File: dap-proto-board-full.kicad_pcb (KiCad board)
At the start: 6 copper layers, 42.2 x 61.4 mm, 102 parts, among them J1 SFV18R-1STE1HLF, J2 UJ20-C-H-G-SMT-1-P16-TR, J3 SJ-3523-SMT, J4 JST_SH_SM03B-SRSS-TB, J5 JST_PH_S2B-PH-SM4, J6 Conn_01x06, J7 Conn_01x08, SW1 B3U-1000P, SW2 B3U-1000P, U1 TPD1E05U06DPY, U10 nPM1300-QEXX, U11 TPS22917DBV, U12 TPS63031DSK, U2 TAD5212, U3 TXS0108ERGYR, U4 W25Q64JWUUIQ, U5 TXS0108ERGYR, U6 MSD-11-A, U7 APS6404L-SQRH-ZR, U8 RP2350A, U9 TLV73311PDBV, Y1 SIT8021AI-J4-XXS-12.288E, Y2 SIT8021AI-J4-XXS-11.289E, Y3 ABM8-272-T3

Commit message: I forgort what I did
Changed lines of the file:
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@@
+	)
+	(segment
+		(start 110.4 81.408102)
+		(end 110.4 81.8)
+		(width 0.150114)
+		(layer "F.Cu")
+		(net "/QSPI_SD2")
+	)
+	(segment
+		(start 109.868955 80.877057)
+		(end 110.4 81.408102)
+		(width 0.150114)
+		(layer "F.Cu")
+		(net "/QSPI_SD2")
 	)
 	(segment
@@
 	)
 	(segment
-		(start 109.868955 80.877057)
-		(end 110.4 81.408102)
-		(width 0.150114)
-		(layer "F.Cu")
-		(net "/QSPI_SD2")
-	)
-	(segment
-		(start 106.470716 80.05722)
-		(end 106.486498 80.073002)
-		(width 0.150114)
-		(layer "F.Cu")
-		(net "/QSPI_SD2")
-	)
-	(segment
-		(start 106.451998 80.073002)
-		(end 106.475 80.05)
+		(start 106.486498 80.073002)
+		(end 106.823874 80.073002)
 		(width 0.150114)
 		(layer "F.Cu")
@@
 	)
 	(segment
-		(start 106.486498 80.073002)
-		(end 106.823874 80.073002)
+		(start 106.486497 80.073001)
+		(end 106.486498 80.073002)
 		(width 0.150114)
 		(layer "F.Cu")
@@
 	)
 	(segment
-		(start 110.4 81.408102)
-		(end 110.4 81.8)
+		(start 106.130949 80.073001)
+		(end 106.486497 80.073001)
+		(width 0.150114)
+		(layer "F.Cu")
+		(net "/QSPI_SD2")
+	)
+	(segment
+		(start 106.451998 80.073002)
+		(end 106.475 80.05)
 		(width 0.150114)
 		(layer "F.Cu")
@@
 	)
 	(via
-		(at 106.470716 80.05722)
+		(at 106.130949 80.073001)
 		(size 0.45)
 		(drill 0.3)
@@
 	)
 	(segment
-		(start 105.973002 80.073002)
-		(end 104 78.1)
+		(start 104 78.1)
+		(end 104 77.55)
 		(width 0.150114)
 		(layer "In2.Cu")
@@
 	)
 	(segment
-		(start 106.470716 80.05722)
-		(end 106.454934 80.073002)
-		(width 0.150114)
-		(layer "In2.Cu")
-		(net "/QSPI_SD2")
-	)
-	(segment
-		(start 106.454934 80.073002)
+		(start 106.130948 80.073002)
 		(end 105.973002 80.073002)
 		(width 0.150114)
@@
 	)
 	(segment
-		(start 104 78.1)
-		(end 104 77.55)
+		(start 106.130949 80.073001)
+		(end 106.130948 80.073002)
 		(width 0.150114)
 		(layer "In2.Cu")
+		(net "/QSPI_SD2")
+	)
+	(segment
+		(start 105.973002 80.073002)
+		(end 104 78.1)
+		(width 0.150114)
+		(layer "In2.Cu")

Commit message: mostly finished; just need to breakout extra gpio
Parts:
- removed C19, C40, C48, C52: 100nF, Capacitor_SMD:C_0402_1005Metric
- removed C41, C43: 10uF, Capacitor_SMD:C_0603_1608Metric
- removed C42, C44: 100nF, Capacitor_SMD:C_0603_1608Metric
- removed C45, C46, C51, C53, C54: 10uF, Capacitor_SMD:C_0402_1005Metric
- removed C47: 2.2uF, Capacitor_SMD:C_0402_1005Metric
- removed C49: 1uF, Capacitor_SMD:C_0402_1005Metric
- removed C50: 1nF, Capacitor_SMD:C_0402_1005Metric
- removed J5: JST_PH_S2B-PH-SM4, Connector_JST:JST_PH_S2B-PH-SM4-TB_1x02-1MP_P2.00mm_Horizontal
- removed J6: Conn_01x06, Connector_PinSocket_2.54mm:PinSocket_1x06_P2.54mm_Vertical
- removed J7: Conn_01x08, Connector_PinSocket_2.54mm:PinSocket_1x08_P2.54mm_Vertical
- removed L1: 2.2uH, Inductor_SMD:L_0603_1608Metric
- removed R14: 4.7k, Resistor_SMD:R_0402_1005Metric
- removed R15: 10, Resistor_SMD:R_0402_1005Metric
- removed R16: 47k, Resistor_SMD:R_0402_1005Metric
- removed R3: 10k, Resistor_SMD:R_0402_1005Metric
- removed U10: nPM1300-QEXX, Package_DFN_QFN:QFN-32-1EP_5x5mm_P0.5mm_EP3.6x3.6mm_ThermalVias
- removed U11: TPS22917DBV, Package_TO_SOT_SMD:SOT-23-6
- removed U12: TPS63031DSK, Package_SON:WSON-10-1EP_2.5x2.5mm_P0.5mm_EP1.2x2mm_ThermalVias
- removed U8: RP2350A, Package_DFN_QFN:QFN-60-1EP_7x7mm_P0.4mm_EP3.4x3.4mm
- removed U9: TLV73311PDBV, Package_TO_SOT_SMD:SOT-23-5
- removed Y2: SIT8021AI-J4-XXS-11.289E, SIT8021AI-J4-XXS-24.000000E:OSC_SIT8021AI-J4-XXS-24.000000E
- removed Y3: ABM8-272-T3, Crystal:Crystal_SMD_3225-4Pin_3.2x2.5mm
- added SW3: B3U-1000P, Button_Switch_SMD:SW_Push_1P1T_NO_Vertical_Wuerth_434133025816, F.Cu at (131.5, 70.1)
- C1, C11, C12, C2, C20, C22, C28, C3, C4, C8, C9: footprint Capacitor_SMD:C_0402_1005Metric -> Capacitor_SMD:C_0603_1608Metric
- C10, C24, C27, C29, C6: value 100nF -> 10uF; footprint Capacitor_SMD:C_0402_1005Metric -> Capacitor_SMD:C_0603_1608Metric
- C13: value 100nF -> 22uF; footprint Capacitor_SMD:C_0402_1005Metric -> Capacitor_SMD:C_0603_1608Metric
- C14: value 10uF -> 10nF; footprint Capacitor_SMD:C_0402_1005Metric -> Capacitor_SMD:C_0603_1608Metric
- C15, C21, C23, C25, C34, C7: value 100nF -> 1uF; footprint Capacitor_SMD:C_0402_1005Metric -> Capacitor_SMD:C_0603_1608Metric
- C16: value 10uF -> 100nF; footprint Capacitor_SMD:C_0402_1005Metric -> Capacitor_SMD:C_0603_1608Metric
- C17: value 1uF -> 18pF; footprint Capacitor_SMD:C_0402_1005Metric -> Capacitor_SMD:C_0603_1608Metric
- C18: value 10nF -> 18pF; footprint Capacitor_SMD:C_0402_1005Metric -> Capacitor_SMD:C_0603_1608Metric
- C26: value 10nF -> 100nF; footprint Capacitor_SMD:C_0402_1005Metric -> Capacitor_SMD:C_0603_1608Metric
- C30: value 15pF -> 100nF; footprint Capacitor_SMD:C_0402_1005Metric -> Capacitor_SMD:C_0603_1608Metric
- C31: value 15pF -> 10uF; footprint Capacitor_SMD:C_0402_1005Metric -> Capacitor_SMD:C_0603_1608Metric
- C32: value 100nF -> 2.2uF; footprint Capacitor_SMD:C_0402_1005Metric -> Capacitor_SMD:C_0603_1608Metric
- C33: value 4.7uF -> 100nF; footprint Capacitor_SMD:C_0402_1005Metric -> Capacitor_SMD:C_0603_1608Metric
- C35: value 10uF -> 1nF; footprint Capacitor_SMD:C_0402_1005Metric -> Capacitor_SMD:C_0603_1608Metric
- C36: value 2.2uF -> 10uF; footprint Capacitor_SMD:C_0402_1005Metric -> Capacitor_SMD:C_0603_1608Metric
- C37: value 1uF -> 100nF; footprint Capacitor_SMD:C_0402_1005Metric -> Capacitor_SMD:C_0603_1608Metric
- C38, C39: value 1uF -> 10uF; footprint Capacitor_SMD:C_0402_1005Metric -> Capacitor_SMD:C_0603_1608Metric
- C5: value 13pF -> 100nF; footprint Capacitor_SMD:C_0402_1005Metric -> Capacitor_SMD:C_0603_1608Metric
- J4: value JST_SH_SM03B-SRSS-TB -> JST_PH_S2B-PH-SM4; footprint Connector_JST:JST_SH_SM03B-SRSS-TB_1x03-1MP_P1.00mm_Horizontal -> Connector_JST:JST_PH_S2B-PH-SM4-TB_1x02-1MP_P2.00mm_Horizontal
- R1: value 100k -> 0; footprint Resistor_SMD:R_0402_1005Metric -> Resistor_SMD:R_0603_1608Metric
- R10, R11, R12: value 4.7k -> 47k; footprint Resistor_SMD:R_0402_1005Metric -> Resistor_SMD:R_0603_1608Metric
- R13: value 1k -> 47k; footprint Resistor_SMD:R_0402_1005Metric -> Resistor_SMD:R_0603_1608Metric
- R2: value 100k -> 10k; footprint Resistor_SMD:R_0402_1005Metric -> Resistor_SMD:R_0603_1608Metric
- R4: value 10k -> 2.2; footprint Resistor_SMD:R_0402_1005Metric -> Resistor_SMD:R_0603_1608Metric
- R5, R6: footprint Resistor_SMD:R_0402_1005Metric -> Resistor_SMD:R_0603_1608Metric
- R7: value 1k -> 10k; footprint Resistor_SMD:R_0402_1005Metric -> Resistor_SMD:R_0603_1608Metric
- R8, R9: value 27 -> 10k; footprint Resistor_SMD:R_0402_1005Metric -> Resistor_SMD:R_0603_1608Metric
- SW1, SW2: value B3U-1000P -> SW_Push; footprint Button_Switch_SMD:SW_SPST_B3U-1000P -> Button_Switch_SMD:SW_Push_1P1T_NO_Vertical_Wuerth_434133025816
- U1: value TPD1E05U06DPY -> MSD-11-A; footprint Package_SON:Texas_DPY0002A_0.6x1mm_P0.65mm -> MSD-11-A:CUI_MSD-11-A
- U2: value TAD5212 -> USBLC6-2SC6; footprint Package_DFN_QFN:TAD5212 -> Package_TO_SOT_SMD:SOT-23-6
- U3: value TXS0108ERGYR -> TAD5212; footprint Package_DFN_QFN:Texas_RGY_R-PVQFN-N20_EP2.05x3.05mm_ThermalVias -> footprints:VQFN24_RGE_CORNERPADS_TEX
- U4: value W25Q64JWUUIQ -> ESP32-S3; footprint Package_SON:Winbond_USON-8-1EP_3x2mm_P0.5mm_EP0.2x1.6mm -> Package_DFN_QFN:QFN-56-1EP_7x7mm_P0.4mm_EP4x4mm_ThermalVias
- U5: value TXS0108ERGYR -> nPM1300-QEXX; footprint Package_DFN_QFN:Texas_RGY_R-PVQFN-N20_EP2.05x3.05mm_ThermalVias -> Package_DFN_QFN:QFN-32-1EP_5x5mm_P0.5mm_EP3.6x3.6mm_ThermalVias
- U6: value MSD-11-A -> TPS22917DBV; footprint MSD-11-A:CUI_MSD-11-A -> Package_TO_SOT_SMD:SOT-23-6
- U7: value APS6404L-SQRH-ZR -> TPS63031DSK; footprint Package_SON:Winbond_USON-8-1EP_3x2mm_P0.5mm_EP0.2x1.6mm -> Package_SON:WSON-10-1EP_2.5x2.5mm_P0.5mm_EP1.2x2mm_ThermalVias
- Y1: value SIT8021AI-J4-XXS-12.288E -> ABM8-40.000MHZ-12-B1U-T; footprint SIT8021AI-J4-XXS-24.000000E:OSC_SIT8021AI-J4-XXS-24.000000E -> Crystal:Crystal_SMD_3225-4Pin_3.2x2.5mm
- moved J4 51.3 mm to (129.6, 62.4)
- moved U1 39.0 mm to (103.1, 103.6)
- moved H2 37.0 mm to (130.7, 75.6)
- moved R4 34.0 mm to (126.7, 105.4)
- moved C9 32.3 mm to (126.7, 101.9), turned to 180 degrees
- moved C31 30.2 mm to (121.2, 64.1), turned to 0 degrees
- moved R2 29.2 mm to (132.3, 87.9)
- moved C35 27.2 mm to (113.9, 101.0), turned to 0 degrees
- moved U2 26.9 mm to (112.6, 66.7)
- moved C33 26.4 mm to (121.2, 65.7), turned to 0 degrees
- moved C26 25.7 mm to (125.4, 70.2), turned to 0 degrees
- moved C32 25.3 mm to (124.4, 66.0), turned to 0 degrees
- moved SW1 23.6 mm to (128.1, 82.2), turned to -90 degrees
- moved U5 23.3 mm to (120.4, 69.8), turned to 90 degrees
- moved U3 22.6 mm to (125.4, 98.4), turned to 180 degrees
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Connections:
- C1 pad 2: +1V8 -> +3V3
- C10 pad 1: +3V3 -> GND
- C10 pad 2: GND -> Net-(U3-AVDD)
- C12 pad 1: Net-(U2-VREF) -> +3V3
- C13 pad 1: GND -> +3V3
- C13 pad 2: +1V8 -> GND
- C14 pad 1: GND -> +3V3
- C14 pad 2: +1V8 -> GND
- C15 pad 1: /SD_VCC -> +3V3
- C16 pad 1: /SD_VCC -> +3V3
- C17 pad 1: +1V8 -> /XOUT
- C18 pad 1: +1V8 -> Net-(C18-Pad1)
- C2 pad 1: +1V8 -> +3V3
- C20 pad 1: GND -> +3V3
- C20 pad 2: +1V8 -> GND
- C21 pad 1: GND -> +3V3
- C21 pad 2: +3V3 -> GND
- C22 pad 1: GND -> +3V3
- C22 pad 2: +1V8 -> GND
- C23 pad 1: GND -> Net-(U4-CHIP_PU)
- C23 pad 2: +1V8 -> GND
- C24 pad 1: GND -> +3V3
- C24 pad 2: +1V8 -> GND
- C25 pad 1: GND -> VBUS
- C25 pad 2: +1V8 -> GND
- C26 pad 1: +1V8 -> +3V3
- C27 pad 1: GND -> VSYS
- C27 pad 2: +1V8 -> GND
- C28 pad 1: GND -> VSYS
- C28 pad 2: +1V8 -> GND
- C29 pad 1: GND -> VSYS
- C29 pad 2: +1V8 -> GND
- C30 pad 1: /XIN -> VSYS
- C31 pad 1: Net-(C31-Pad1) -> VSYS
- C32 pad 1: +1V1 -> +BATT
- C33 pad 1: +1V1 -> VSYS
- C34 pad 1: +1V1 -> Net-(U5-VBUSOUT)
- C35 pad 1: +1V8 -> +3V3
- C35 pad 2: GND -> Net-(U6-CT)
- C36 pad 1: /VREG_AVDD -> VSYS
- C37 pad 1: VBUS -> Net-(U7-EN)
- C38 pad 1: +1V8 -> +3V3
- C39 pad 1: +1V1 -> +3V3
- C5 pad 1: /GPO1 -> SD_VCC
- C5 pad 2: Net-(U2-GPO1) -> GND
- C6 pad 1: +1V8 -> SD_VCC
- C7 pad 1: +1V8 -> Net-(U3-MICBIAS)
- C8 pad 1: Net-(U2-MICBIAS) -> Net-(U3-VREF)
- C9 pad 1: +1V8 -> GND
- C9 pad 2: GND -> Net-(U3-AVDD)
- D1 pad 2: +1V8 -> +3V3
- D2 pad 2: +1V8 -> +3V3
- J1 pad 13: /disp_CS_SCL -> /disp_SCL
- J1 pad 14: /disp_DC_SDA -> /disp_SDA
- J1 pad 4: /disp_SCK -> /disp_SCLK
- J1 pad 7: /disp_DC_SDA -> /disp_DC
- J1 pad 9: /disp_CS_SCL -> /disp_CS
- J2 pad A6: /USB_D+ -> Net-(J2-D+-PadA6)
- J2 pad A7: /USB_D- -> Net-(J2-D--PadA7)
- J2 pad B6: /USB_D+ -> Net-(J2-D+-PadA6)
- J2 pad B7: /USB_D- -> Net-(J2-D--PadA7)
- J4 pad 1: /SWCLK -> +BATT
- L2 pad 1: Net-(U12-L1) -> Net-(U7-L1)
- L2 pad 2: Net-(U12-L2) -> Net-(U7-L2)
- R1 pad 1: /SD_ON -> /XIN
- R1 pad 2: GND -> Net-(C18-Pad1)
- R10 pad 1: +1V8 -> +3V3
- R10 pad 2: /npm_SDA -> /npm_SCL
- R11 pad 1: +1V8 -> +3V3
- R11 pad 2: /npm_SCL -> /npm_SDA
- R12 pad 1: +1V8 -> +3V3
- R13 pad 1: /XOUT -> +3V3
- R13 pad 2: Net-(C31-Pad1) -> /tad_SCL
- R2 pad 1: /DISP_IO_ON -> +3V3
- R2 pad 2: GND -> Net-(U4-CHIP_PU)
- R4 pad 1: +1V8 -> +3V3
- R4 pad 2: /PSRAM_CS -> Net-(U3-AVDD)
- R5 pad 1: +1V8 -> +3V3
- R5 pad 2: /DIS_CLK1 -> /SD_DAT2
- R6 pad 1: +1V8 -> +3V3
- R6 pad 2: /DIS_CLK2 -> /SD_CS
- R7 pad 1: /FLASH_CS -> +3V3
- R7 pad 2: /~{USB_BOOT} -> /SD_DIN
- R8 pad 1: /USB_D- -> +3V3
- R8 pad 2: Net-(U8-USB_DM) -> /SD_DOUT
- R9 pad 1: /USB_D+ -> +3V3
- R9 pad 2: Net-(U8-USB_DP) -> /SD_DAT1
- SW1 pad 2: /~{USB_BOOT} -> Net-(U4-GPIO0)
- SW2 pad 1: /SHPHLD -> Net-(U4-CHIP_PU)
- U1 pad 1: GND -> /SD_DAT2
- U1 pad 2: VBUS -> /SD_CS
- U2 pad 1: /DREG -> Net-(J2-D--PadA7)
- U2 pad 2: /BCLK -> GND
- U2 pad 3: /FSYNC -> Net-(J2-D+-PadA6)
- U2 pad 4: /DOUT -> /USB_D+
- U2 pad 5: /DIN -> VBUS
- U2 pad 6: +1V8 -> /USB_D-
- U3 pad 1: /SD_DAT2 -> /DREG
- U3 pad 10: /SD_ON -> /tad_GPIO2
- U3 pad 11: GND -> /tad_GPO1
- U3 pad 12: unconnected-(U3-B8-Pad12) -> /tad_GPI1
- U3 pad 13: unconnected-(U3-B7-Pad13) -> GND
- U3 pad 14: /3v_SD_DAT1 -> Net-(U3-MICBIAS)
- U3 pad 15: /3v_SD_DOUT -> GND
- U3 pad 16: /3v_SD_SCLK -> GND
- U3 pad 17: /3v_SD_DIN -> GND
- U3 pad 18: /3v_SD_CS -> GND
- U3 pad 19: +3V3 -> VCOM
- U3 pad 2: +1V8 -> /BCLK
- U3 pad 20: /3v_SD_DAT2 -> /OUT1P
- U3 pad 21: GND -> /OUT2P
- U3 pad 3: /SD_CS -> /FSYNC
- U3 pad 4: /SD_DIN -> /DOUT
- U3 pad 5: /SD_SCLK -> /DIN
- U3 pad 6: /SD_DOUT -> +3V3
- U3 pad 7: /SD_DAT1 -> /tad_SCL
- U3 pad 8: unconnected-(U3-A7-Pad8) -> /tad_SDA
- U3 pad 9: unconnected-(U3-A8-Pad9) -> /tad_GPIO1
- U4 pad 1: /FLASH_CS -> unconnected-(U4-LNA_IN-Pad1)
- U4 pad 2: /QSPI_SD1 -> +3V3
- U4 pad 3: /QSPI_SD2 -> +3V3
- U4 pad 4: GND -> Net-(U4-CHIP_PU)
- U4 pad 5: /QSPI_SD0 -> Net-(U4-GPIO0)
- U4 pad 6: /QSPI_SCLK -> /tad_SDA
- U4 pad 7: /QSPI_SD3 -> /tad_SCL
- U4 pad 8: +1V8 -> unconnected-(U4-GPIO3-Pad8)
- U4 pad 9: GND -> /DIN
- U5 pad 1: unconnected-(U5-A1-Pad1) -> VSYS
- U5 pad 10: /DISP_IO_ON -> /npm_GPIO3
- U5 pad 11: GND -> /npm_GPIO4
- U5 pad 12: /disp_LITE -> +3V3
- U5 pad 13: /disp_SCK -> /npm_SDA
- U5 pad 14: /disp_MOSI -> /npm_SCL
- U5 pad 15: /disp_MISO -> /SHPHLD
- U5 pad 16: /disp_DC_SDA -> GND
- U5 pad 17: /disp_CS_SCL -> GND
- U5 pad 18: unconnected-(U5-B2-Pad18) -> GND
- U5 pad 19: +3V3 -> +BATT
- U5 pad 2: +1V8 -> GND
- U5 pad 20: unconnected-(U5-B1-Pad20) -> VSYS
- U5 pad 21: GND -> VBUS
- U5 pad 4: /mcu_disp_CS_SCL -> VSYS
- U5 pad 5: /mcu_dsp_DC_SDA -> unconnected-(U5-SW2-Pad5)
- U5 pad 6: /mcu_disp_MISO -> GND
- U5 pad 7: /mcu_disp_MOSI -> /npm_GPIO0
- U5 pad 8: /mcu_disp_SCK -> /npm_GPIO1
- U5 pad 9: /mcu_disp_LITE -> /npm_GPIO2
- U6 pad 1: /3v_SD_DAT2 -> +3V3
- U6 pad 2: /3v_SD_CS -> GND
- U6 pad 3: /3v_SD_DIN -> /SD_ON
- U6 pad 4: /SD_VCC -> Net-(U6-CT)
- U6 pad 5: /3v_SD_SCLK -> SD_VCC
- U6 pad 6: GND -> SD_VCC
- U7 pad 1: /PSRAM_CS -> +3V3
- U7 pad 2: /QSPI_SD1 -> Net-(U7-L2)
- U7 pad 3: /QSPI_SD2 -> GND
- U7 pad 4: GND -> Net-(U7-L1)
- U7 pad 5: /QSPI_SD0 -> VSYS
- U7 pad 6: /QSPI_SCLK -> Net-(U7-EN)
- U7 pad 7: /QSPI_SD3 -> Net-(U7-EN)
- U7 pad 8: +1V8 -> Net-(U7-EN)
- Y1 pad 1: /DIS_CLK1 -> /XOUT
- Y1 pad 2: /GPO1 -> GND
- Y1 pad 3: +1V8 -> Net-(C18-Pad1)
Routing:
- net GND: track 58.3 -> 117.2 mm, vias 133 -> 67
- net +1V8: track 54.1 -> 0.00 mm, vias 35 -> 0
- net /DOUT: track 0.00 -> 33.2 mm
- net /SWCLK: track 32.9 -> 0.00 mm, vias 2 -> 0
- net /SWD: track 30.6 -> 0.00 mm, vias 2 -> 0
- net Net-(U4-CHIP_PU): track 0.00 -> 26.2 mm, vias 0 -> 2
- net /GPIO11: track 26.2 -> 0.00 mm, vias 1 -> 0
- net /GPIO10: track 24.2 -> 0.00 mm
- net /npm_GPIO0: track 22.5 -> 0.00 mm, vias 3 -> 0
- net +3V3: track 9.59 -> 31.9 mm, vias 16 -> 28
- net /BCLK: track 15.4 -> 37.5 mm
- net /GPIO25: track 21.2 -> 0.00 mm, vias 1 -> 0
- net /GPIO26_ADC0: track 21.1 -> 0.00 mm, vias 1 -> 0
- net /FSYNC: track 14.5 -> 35.4 mm
- net /GPIO9: track 22.2 -> 1.58 mm, vias 0 -> 1
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- added copper zone on F.Cu, net /DREG
- added copper zone on F.Cu, net Net-(U3-AVDD)
- added copper zone on F.Cu, net Net-(U3-VREF)
- added copper zone on F.Cu, net SD_VCC
- added copper zone on In2.Cu, net SD_VCC
- added copper zone on In2.Cu, net VSYS
- removed copper zone on In4.Cu, net +1V1
- removed copper zone on F.Cu, net +1V8
- removed copper zone on In4.Cu, net +1V8
- removed copper zone on F.Cu, net +BATT
- removed copper zone on In2.Cu, net /SD_VCC
- removed copper zone on In3.Cu, net GND
- removed copper zone on F.Cu, net VCOM
- removed copper zone on In2.Cu, net VCOM
- removed copper zone on In4.Cu, net VSYS
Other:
- copper layers 6 -> 4
- board text added: "Full DAP Proto Board v2 2026 Isaiah Gamble"
- board text removed: "DEBUG"
- board text removed: "Full DAP Proto Board v1 2026 Isaiah Gamble"

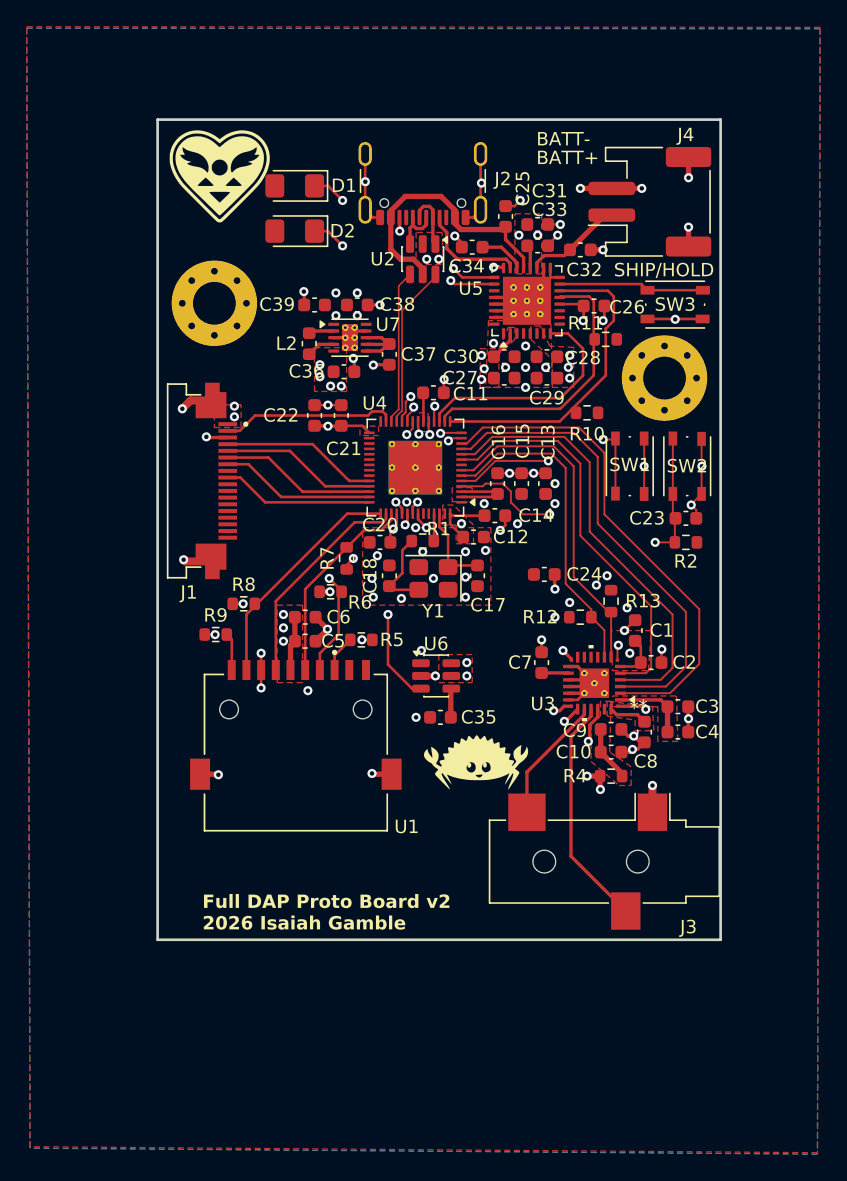
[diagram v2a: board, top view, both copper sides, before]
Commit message: breakout extra gpios; gen gerbers and images
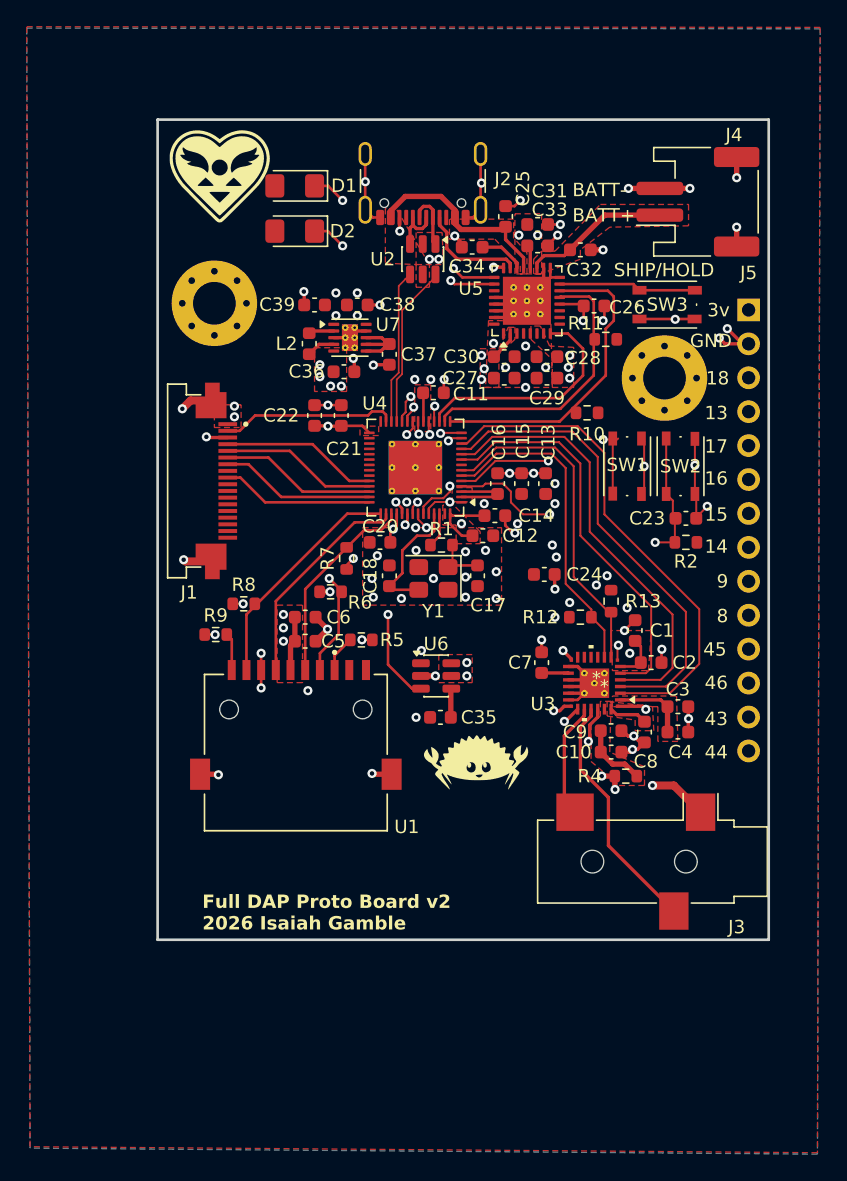
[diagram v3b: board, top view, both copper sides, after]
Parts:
- added J5: Conn_01x14, Connector_PinSocket_2.54mm:PinSocket_1x14_P2.54mm_Vertical, F.Cu at (137.0, 70.5)
- moved J3 3.60 mm to (129.8, 111.8)
- moved J4 3.60 mm to (133.2, 62.4)
- moved R1 1.43 mm to (114.0, 88.1), turned to 0 degrees
- moved R4 1.10 mm to (127.8, 105.4)
- moved C12 0.71 mm to (117.1, 87.4)
- moved SW3 0.60 mm to (130.9, 70.1)
- moved SW2 0.50 mm to (131.9, 82.2)
- moved SW1 0.20 mm to (127.9, 82.2)
- moved C9 0.10 mm to (126.7, 102.0)
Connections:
- C17 pad 1: /XOUT -> Net-(C17-Pad1)
- C18 pad 1: Net-(C18-Pad1) -> /XIN
- R1 pad 1: /XIN -> /XOUT
- R1 pad 2: Net-(C18-Pad1) -> Net-(C17-Pad1)
- Y1 pad 1: /XOUT -> Net-(C17-Pad1)
- Y1 pad 3: Net-(C18-Pad1) -> /XIN
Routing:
- net /GPIO43: track 1.02 -> 35.8 mm
- net /GPIO44: track 1.31 -> 34.3 mm
- net /GPIO45: track 0.00 -> 30.8 mm, vias 0 -> 1
- net /GPIO46: track 0.00 -> 30.2 mm, vias 0 -> 1
- net /GPIO8: track 1.06 -> 29.8 mm
- net /GPIO14: track 1.01 -> 29.5 mm
- net /GPIO9: track 1.58 -> 29.7 mm
- net /GPIO16: track 1.17 -> 29.1 mm
- net /GPIO15: track 0.97 -> 28.8 mm
- net /GPIO18: track 2.13 -> 29.7 mm
- net /GPIO17: track 1.27 -> 27.5 mm
- net /GPIO13: track 1.17 -> 25.8 mm
- net /XIN: track 2.06 -> 9.67 mm
- net Net-(C18-Pad1): track 6.38 -> 0.00 mm
- net GND: track 117.2 -> 123.0 mm, vias 67 -> 71
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- added copper zone on F.Cu, net +BATT
- added copper zone on F.Cu, net VBUS
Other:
- board size 42.2 x 61.4 mm -> 45.8 x 61.4 mm
- board text added: "13"
- board text added: "14"
- board text added: "15"
- board text added: "16"
- board text added: "17"
- board text added: "18"
- board text added: "3v"
- board text added: "43"
- board text added: "44"
- board text added: "45"
- board text added: "46"
- board text added: "8"
- board text removed: "10"
- board text removed: "11"
- board text removed: "1v8"
- board text removed: "22"
- board text removed: "23"
- board text removed: "24"
- board text removed: "25"
- board text removed: "26"
- board text removed: "3v3"
